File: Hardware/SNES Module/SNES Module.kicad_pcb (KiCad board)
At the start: 2 copper layers, 63.5 x 95.5 mm, 4 parts, among them J1 Conn_01x31_Pin, J2 Conn_01x31_Pin

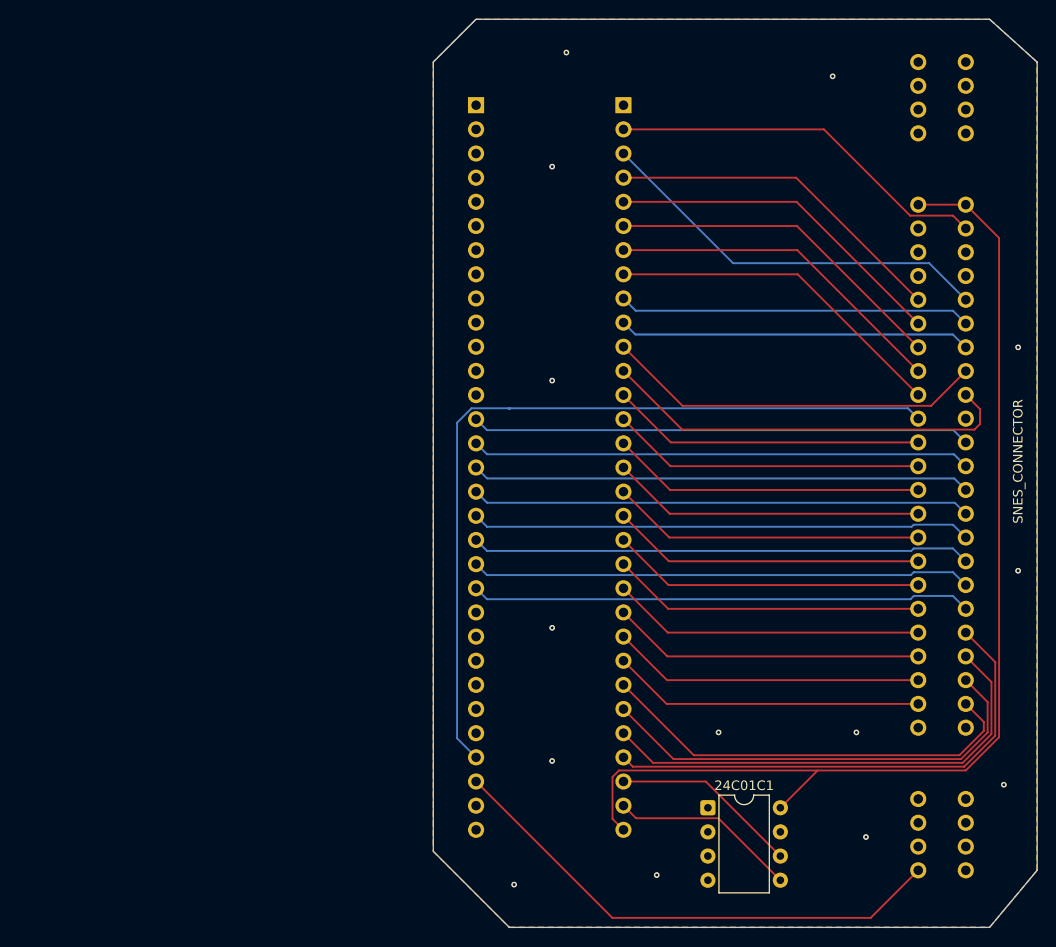
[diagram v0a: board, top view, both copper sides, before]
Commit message: Setup Check Health menu, and remade the SNES Module PCB.
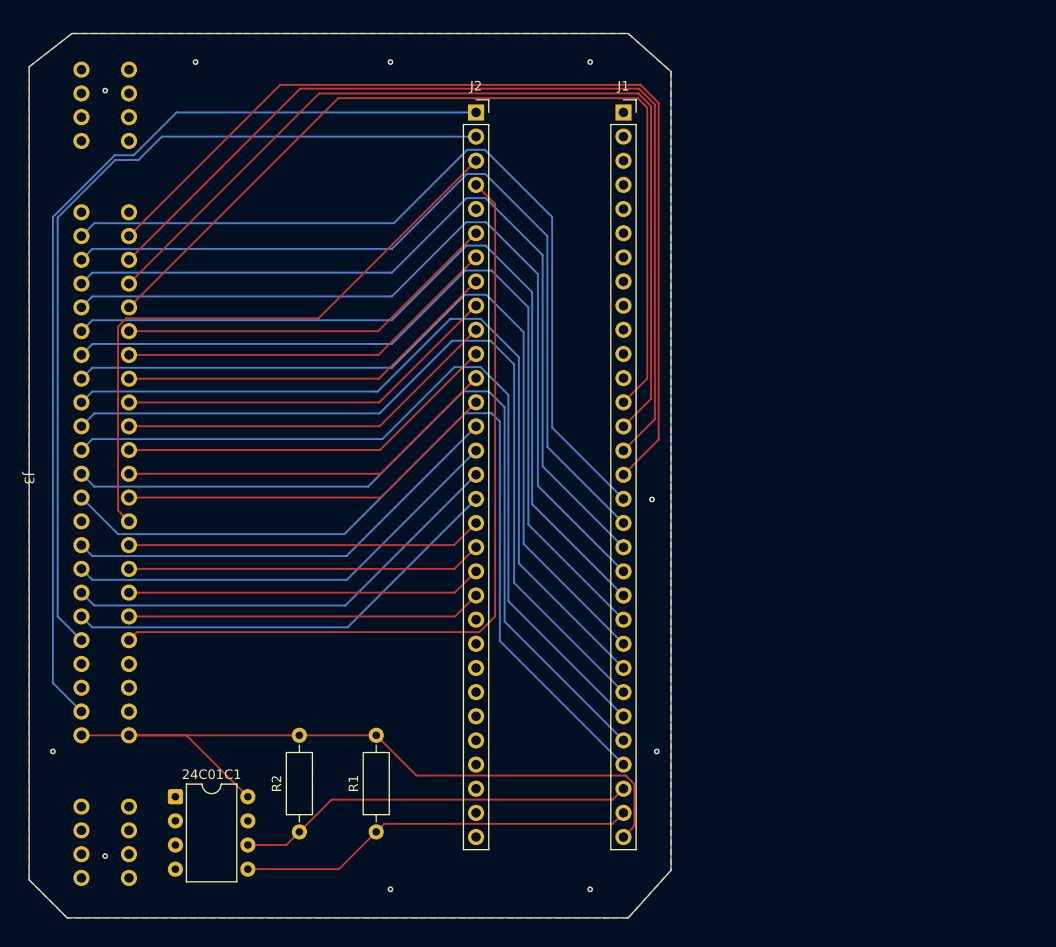
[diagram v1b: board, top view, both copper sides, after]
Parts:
- added R1: R, Resistor_THT:R_Axial_DIN0207_L6.3mm_D2.5mm_P10.16mm_Horizontal, F.Cu at (136.0, 118.0)
- added R2: R, Resistor_THT:R_Axial_DIN0207_L6.3mm_D2.5mm_P10.16mm_Horizontal, F.Cu at (127.9, 118.0)
- J1, J2: footprint Connector_PinHeader_2.54mm:PinHeader_1x31_P2.54mm_Vertical -> Connector_PinSocket_2.54mm:PinSocket_1x31_P2.54mm_Vertical; moved to F.Cu
- moved J3 131.0 mm to (105.0, 33.8), turned to 0 degrees
- moved 24C01C1 56.0 mm to (114.9, 114.3)
- moved J1 0.76 mm to (162.0, 42.3), turned to 0 degrees
- moved J2 0.76 mm to (146.5, 42.3), turned to 0 degrees
- renumbered SNES_CONNECTOR to J3
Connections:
- 24C01C1 pad 1: unconnected-(24C01C1-A0-Pad1) -> GND
- 24C01C1 pad 2: unconnected-(24C01C1-A1-Pad2) -> GND
- 24C01C1 pad 3: unconnected-(24C01C1-A2-Pad3) -> GND
- J1 pad 10: Net-(J1-Pin_10) -> unconnected-(J1-Pin_10-Pad10)
- J1 pad 11: Net-(J1-Pin_11) -> unconnected-(J1-Pin_11-Pad11)
- J1 pad 12: Net-(J1-Pin_12) -> unconnected-(J1-Pin_12-Pad12)
- J1 pad 2: Net-(J1-Pin_2) -> unconnected-(J1-Pin_2-Pad2)
- J1 pad 3: Net-(J1-Pin_3) -> unconnected-(J1-Pin_3-Pad3)
- J1 pad 4: Net-(J1-Pin_4) -> unconnected-(J1-Pin_4-Pad4)
- J1 pad 5: Net-(J1-Pin_5) -> unconnected-(J1-Pin_5-Pad5)
- J1 pad 6: Net-(J1-Pin_6) -> unconnected-(J1-Pin_6-Pad6)
- J1 pad 7: Net-(J1-Pin_7) -> unconnected-(J1-Pin_7-Pad7)
- J1 pad 8: Net-(J1-Pin_8) -> unconnected-(J1-Pin_8-Pad8)
- J1 pad 9: Net-(J1-Pin_9) -> unconnected-(J1-Pin_9-Pad9)
- J2 pad 1: unconnected-(J2-Pin_1-Pad1) -> Net-(J2-Pin_1)
- J2 pad 10: unconnected-(J2-Pin_10-Pad10) -> Net-(J2-Pin_10)
- J2 pad 11: unconnected-(J2-Pin_11-Pad11) -> Net-(J2-Pin_11)
- J2 pad 12: unconnected-(J2-Pin_12-Pad12) -> Net-(J2-Pin_12)
- J2 pad 13: unconnected-(J2-Pin_13-Pad13) -> Net-(J2-Pin_13)
- J2 pad 2: unconnected-(J2-Pin_2-Pad2) -> Net-(J2-Pin_2)
- J2 pad 28: Net-(J2-Pin_28) -> unconnected-(J2-Pin_28-Pad28)
- J2 pad 29: Net-(J2-Pin_29) -> unconnected-(J2-Pin_29-Pad29)
- J2 pad 3: unconnected-(J2-Pin_3-Pad3) -> Net-(J2-Pin_3)
- J2 pad 4: unconnected-(J2-Pin_4-Pad4) -> Net-(J2-Pin_4)
- J2 pad 6: unconnected-(J2-Pin_6-Pad6) -> Net-(J2-Pin_6)
- J2 pad 7: unconnected-(J2-Pin_7-Pad7) -> Net-(J2-Pin_7)
- J2 pad 8: unconnected-(J2-Pin_8-Pad8) -> Net-(J2-Pin_8)
- J2 pad 9: unconnected-(J2-Pin_9-Pad9) -> Net-(J2-Pin_9)
- J3 pad 10: Net-(J2-Pin_21) -> Net-(J1-Pin_21)
- J3 pad 11: Net-(J2-Pin_20) -> Net-(J1-Pin_22)
- J3 pad 12: Net-(J2-Pin_19) -> Net-(J1-Pin_23)
- J3 pad 13: Net-(J2-Pin_18) -> Net-(J1-Pin_24)
- J3 pad 14: Net-(J2-Pin_17) -> Net-(J1-Pin_25)
- J3 pad 15: Net-(J2-Pin_16) -> Net-(J1-Pin_26)
- J3 pad 16: Net-(J2-Pin_15) -> Net-(J1-Pin_27)
- J3 pad 17: Net-(J2-Pin_14) -> Net-(J1-Pin_28)
- J3 pad 19: Net-(J1-Pin_12) -> Net-(J2-Pin_14)
- J3 pad 20: Net-(J1-Pin_11) -> Net-(J2-Pin_15)
- J3 pad 21: Net-(J1-Pin_10) -> Net-(J2-Pin_16)
- J3 pad 22: Net-(J1-Pin_9) -> Net-(J2-Pin_17)
- J3 pad 23: Net-(J1-Pin_3) -> Net-(J2-Pin_2)
- J3 pad 26: Net-(J1-Pin_2) -> Net-(J2-Pin_1)
- J3 pad 32: Net-(J2-Pin_29) -> unconnected-(J3-Pin_32-Pad32)
- J3 pad 37: Net-(J1-Pin_24) -> Net-(J1-Pin_16)
- J3 pad 38: Net-(J1-Pin_23) -> Net-(J1-Pin_15)
- J3 pad 39: Net-(J1-Pin_22) -> Net-(J1-Pin_14)
- J3 pad 40: Net-(J1-Pin_21) -> Net-(J1-Pin_13)
- J3 pad 41: Net-(J1-Pin_20) -> Net-(J2-Pin_6)
- J3 pad 42: Net-(J1-Pin_19) -> Net-(J2-Pin_7)
- J3 pad 43: Net-(J1-Pin_18) -> Net-(J2-Pin_8)
- J3 pad 44: Net-(J1-Pin_17) -> Net-(J2-Pin_9)
- J3 pad 45: Net-(J1-Pin_16) -> Net-(J2-Pin_10)
- J3 pad 46: Net-(J1-Pin_15) -> Net-(J2-Pin_11)
- J3 pad 47: Net-(J1-Pin_14) -> Net-(J2-Pin_12)
- J3 pad 48: Net-(J1-Pin_13) -> Net-(J2-Pin_13)
- J3 pad 49: Net-(J2-Pin_28) -> Net-(J2-Pin_3)
- J3 pad 50: Net-(J1-Pin_8) -> Net-(J2-Pin_18)
- J3 pad 51: Net-(J1-Pin_7) -> Net-(J2-Pin_19)
- J3 pad 52: Net-(J1-Pin_6) -> Net-(J2-Pin_20)
- J3 pad 53: Net-(J1-Pin_5) -> Net-(J2-Pin_21)
- J3 pad 54: Net-(J1-Pin_4) -> Net-(J2-Pin_4)
- J3 pad 6: Net-(J1-Pin_25) -> Net-(J1-Pin_17)
- J3 pad 7: Net-(J1-Pin_26) -> Net-(J1-Pin_18)
- J3 pad 8: Net-(J1-Pin_27) -> Net-(J1-Pin_19)
- J3 pad 9: Net-(J1-Pin_28) -> Net-(J1-Pin_20)
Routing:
- net Net-(J2-Pin_1): track 0.00 -> 102.3 mm
- net Net-(J2-Pin_2): track 0.00 -> 93.0 mm
- net Net-(J2-Pin_4): track 0.00 -> 85.7 mm
- net Net-(J2-Pin_28): track 85.7 -> 0.00 mm
- net Net-(J1-Pin_16): track 33.0 -> 103.7 mm
- net Net-(J1-Pin_15): track 33.0 -> 101.2 mm
- net Net-(J2-Pin_3): track 0.00 -> 65.8 mm
- net Net-(J1-Pin_14): track 33.0 -> 98.6 mm
- net Net-(J1-Pin_13): track 33.1 -> 96.0 mm
- net Net-(J1-Pin_22): track 32.9 -> 89.3 mm
- net Net-(J1-Pin_21): track 32.9 -> 89.0 mm
- net Net-(J1-Pin_23): track 32.9 -> 88.9 mm
- net Net-(J1-Pin_20): track 32.9 -> 89.0 mm
- net Net-(J1-Pin_19): track 33.0 -> 88.9 mm
- net Net-(J1-Pin_18): track 33.0 -> 88.9 mm
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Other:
- board size 63.5 x 95.5 mm -> 67.5 x 93 mm
